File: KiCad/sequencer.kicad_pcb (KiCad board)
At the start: 2 copper layers, 79.9 x 100 mm, 127 parts, among them J1 CLOCK OUT, J2 GATE OUT, J3 CLOCK IN, J4 CV OUT, J5 RESET, J6 10-pin power header, Q1 BC848W, Q2 MMBT3904, Q3 MMBT3904, Q4 MMBT3904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

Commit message: finalizing silkscreen
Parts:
- removed the G*** at (171.4, 79.0)
- added G***: LOGO, Eurorack:RoHs, F.Cu at (130.9, 101.2)
- added G***: LOGO, LOGO, B.Cu at (114.8, 135.0)
- added G***: LOGO, LOGO, F.Cu at (147.7, 102.7)
- added G***: LOGO, LOGO, F.Cu at (149.6, 125.8)
- added G***: LOGO, LOGO, B.Cu at (114.8, 46.9)
- added G***: LOGO, LOGO, B.Cu at (185.3, 46.9)
- added G***: LOGO, LOGO, B.Cu at (123.9, 53.1)
- added G***: LOGO, LOGO, B.Cu at (185.3, 135.0)
- added G***: LOGO, LOGO, B.Cu at (128.4, 90.4)
- added REF**: WEEE-Logo_4.2x6mm_SilkScreen, Symbol:WEEE-Logo_4.2x6mm_SilkScreen, F.Cu at (130.9, 109.1)
- added REF**: CE-Logo_8.5x6mm_SilkScreen, Symbol:CE-Logo_8.5x6mm_SilkScreen, F.Cu at (132.1, 116.9)
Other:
- board text added: "Designed in South Tyrol"
- board text added: "ID:"
- board text added: "Modulo-8 Sequencer"
- board text added: "REV 1.0"
- board text added: "© Nathanael Noir 2026"

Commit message: adding a README.md
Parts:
- removed the G*** at (149.6, 125.8)
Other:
- board text added: "ALL THIS HAS HAPPENED BEFORE, AND WILL HAPPEN AGAIN"
- board text added: "THE END IS WHERE WE START FROM"
- board text added: "WHERE IT RETURNS, ZENZI"
- board text added: "x_{n+1} ≡ x_{n} + 1 mod 8"

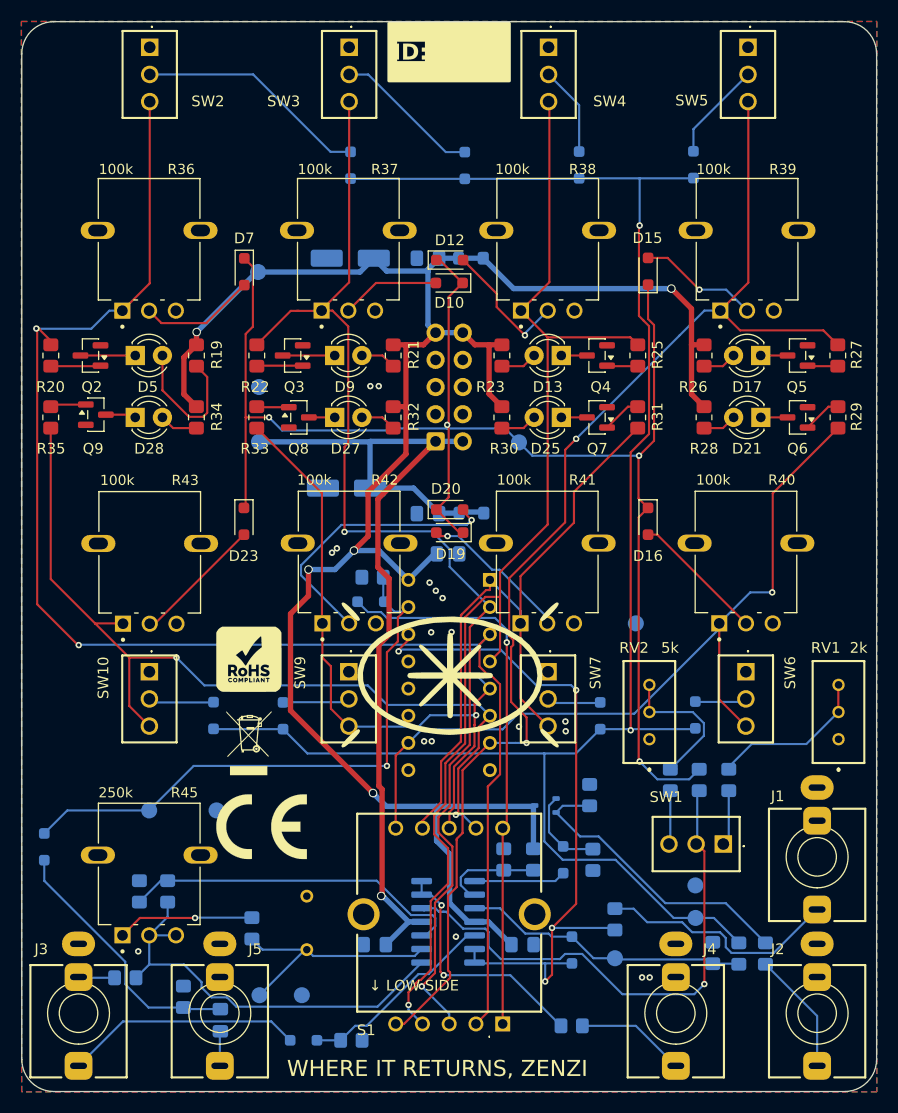
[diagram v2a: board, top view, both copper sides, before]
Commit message: adding qr code
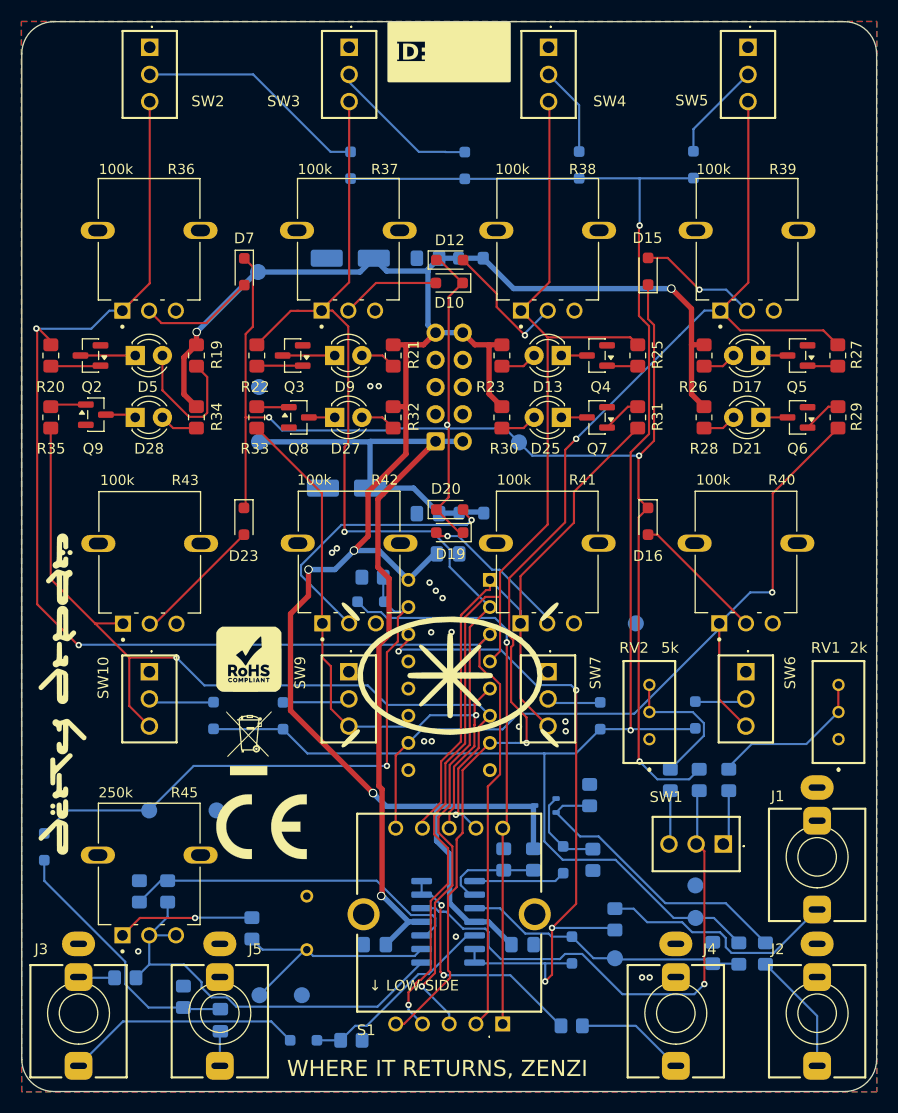
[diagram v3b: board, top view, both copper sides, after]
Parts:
- added G***: LOGO, LOGO, F.Cu at (113.5, 104.5)
- added G***: LOGO, LOGO, B.Cu at (149.6, 47.3)
- added G***: LOGO, LOGO, B.Cu at (168.4, 73.6)
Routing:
- net /CD4017BE/Count6: track 59.9 -> 58.4 mm
- net Net-(SW1-C): track 5.82 -> 5.20 mm
- net GND: track 0.59 -> 0.00 mm
- net Net-(R14-Pad1): track 14.2 -> 13.7 mm
- net Net-(D28-K): track 3.41 -> 2.85 mm
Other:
- board text added: "Do not lick!"
- board text added: "This cap is very large"

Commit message: new logo, via correction, gerber
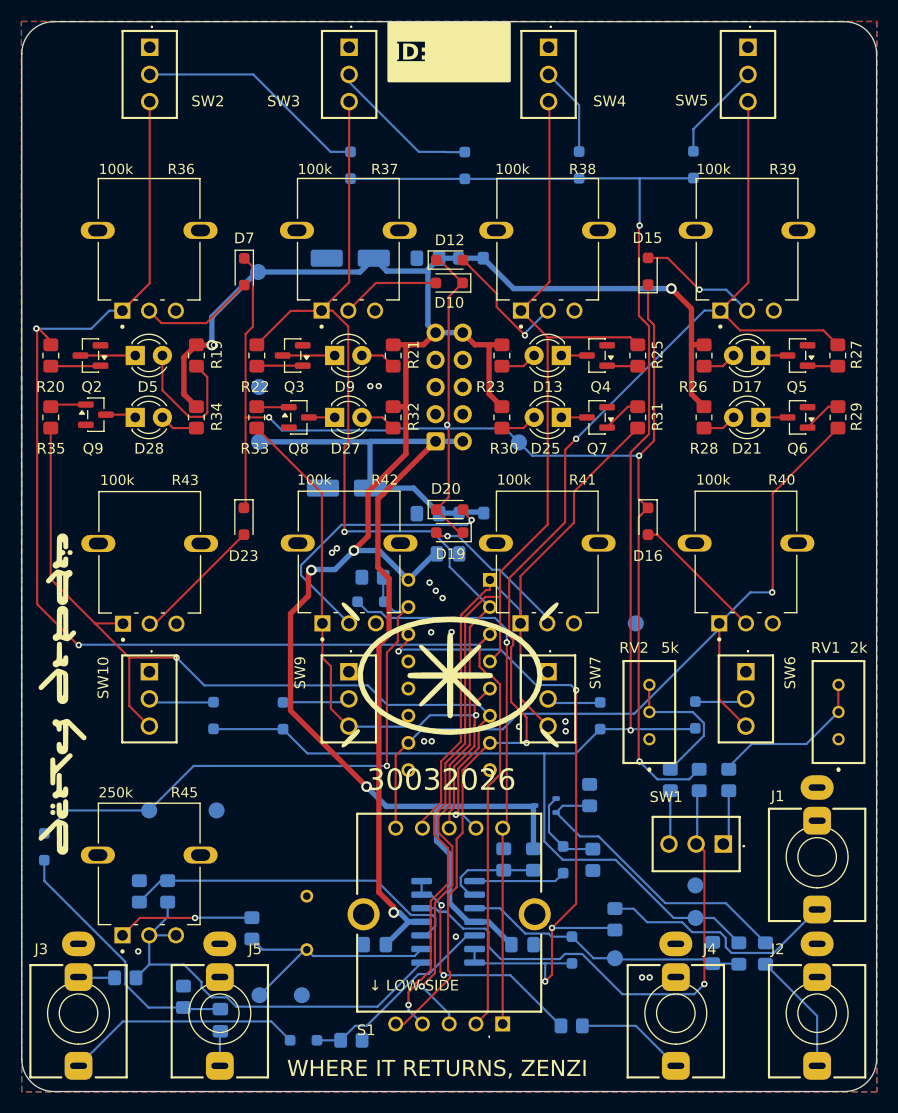
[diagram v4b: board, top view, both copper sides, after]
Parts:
- removed the G*** at (130.9, 101.2)
- removed REF**: WEEE-Logo_4.2x6mm_SilkScreen, Symbol:WEEE-Logo_4.2x6mm_SilkScreen
- removed REF**: CE-Logo_8.5x6mm_SilkScreen, Symbol:CE-Logo_8.5x6mm_SilkScreen
- added G***: LOGO, LOGO, B.Cu at (175.1, 64.6)
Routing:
- net +12V: track 192.9 -> 193.6 mm
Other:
- board text added: "30032026"
